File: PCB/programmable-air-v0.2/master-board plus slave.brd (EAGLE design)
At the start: 97.8 x 98.9 mm, 74 parts, among them IC2 INA126U, IC4 LM358MX, J1 POWER_JACKTOE, Q4 600mA/40V, Q5 600mA/40V, Q6 600mA/40V

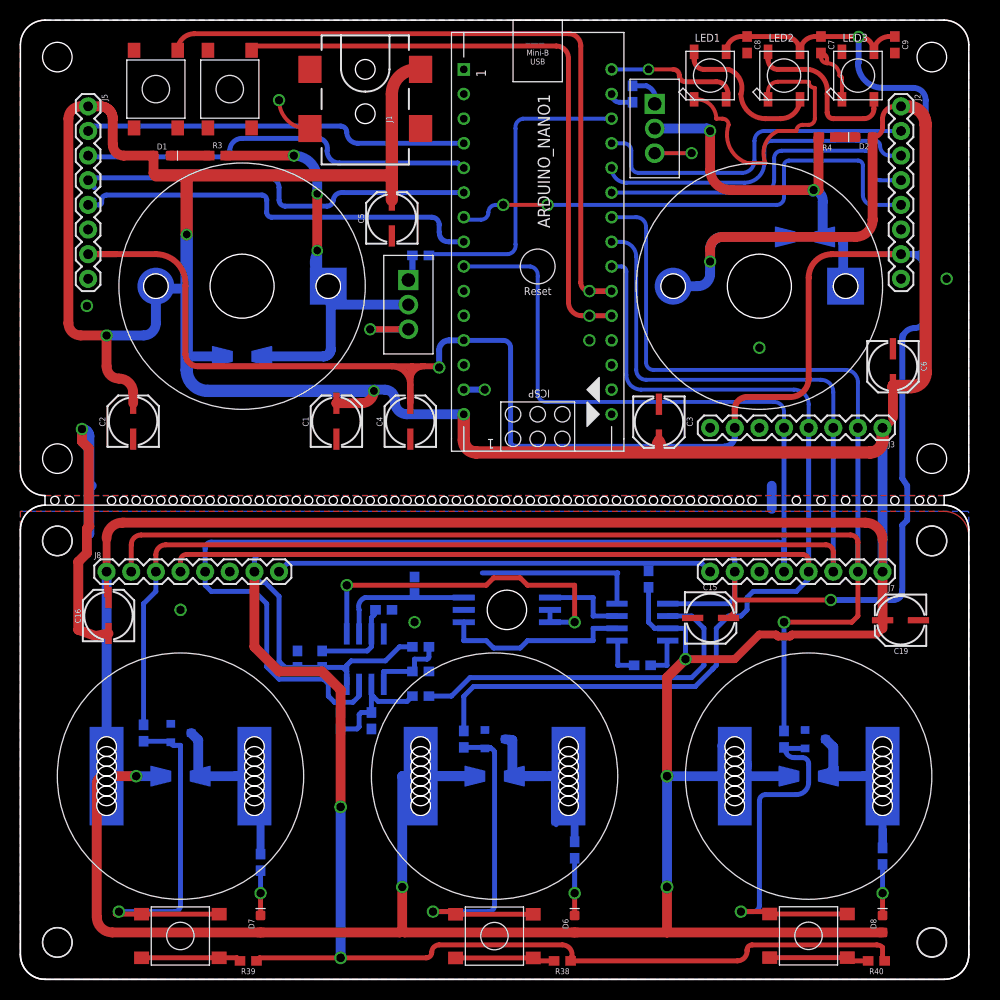
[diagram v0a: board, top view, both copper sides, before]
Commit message: Minor changes to the PCB
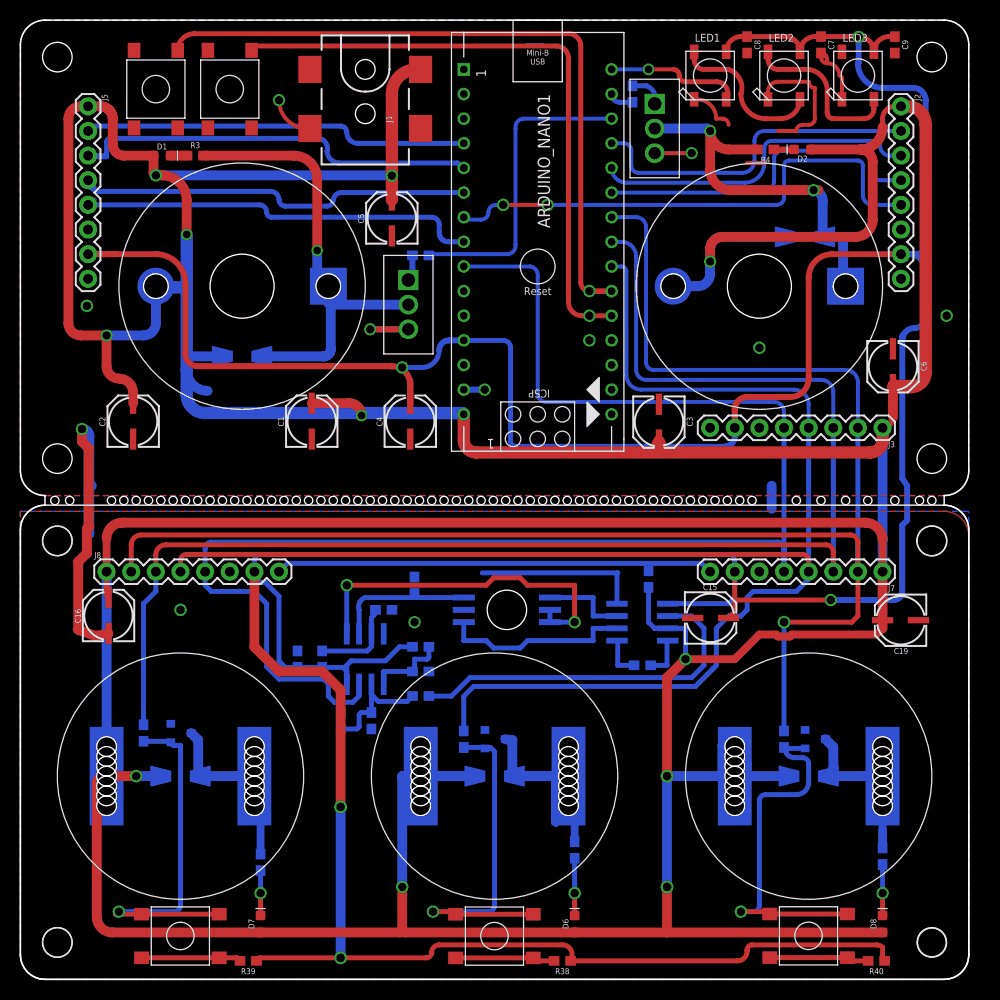
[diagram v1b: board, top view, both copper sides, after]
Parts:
- moved D2 6.48 mm to (80.6, 85.6)
- moved R4 6.48 mm to (76.8, 85.6)
- moved C1 2.54 mm to (29.8, 57.5)
- moved R3 2.29 mm to (18.0, 85.0)
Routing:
- net VCC: track 476.4 -> 468.2 mm
- net GND: track 171.0 -> 163.1 mm
- net VIN: track 797.3 -> 789.6 mm, vias 9 -> 11
- net N$11: track 41.0 -> 43.9 mm
- net N$12: track 3.99 -> 1.70 mm
- net N$14: track 47.5 -> 45.8 mm
- net N$18: track 42.3 -> 41.7 mm
- net N$5: track 49.3 -> 49.2 mm, vias 3 -> 1

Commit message: Sent PCBs for fabrication
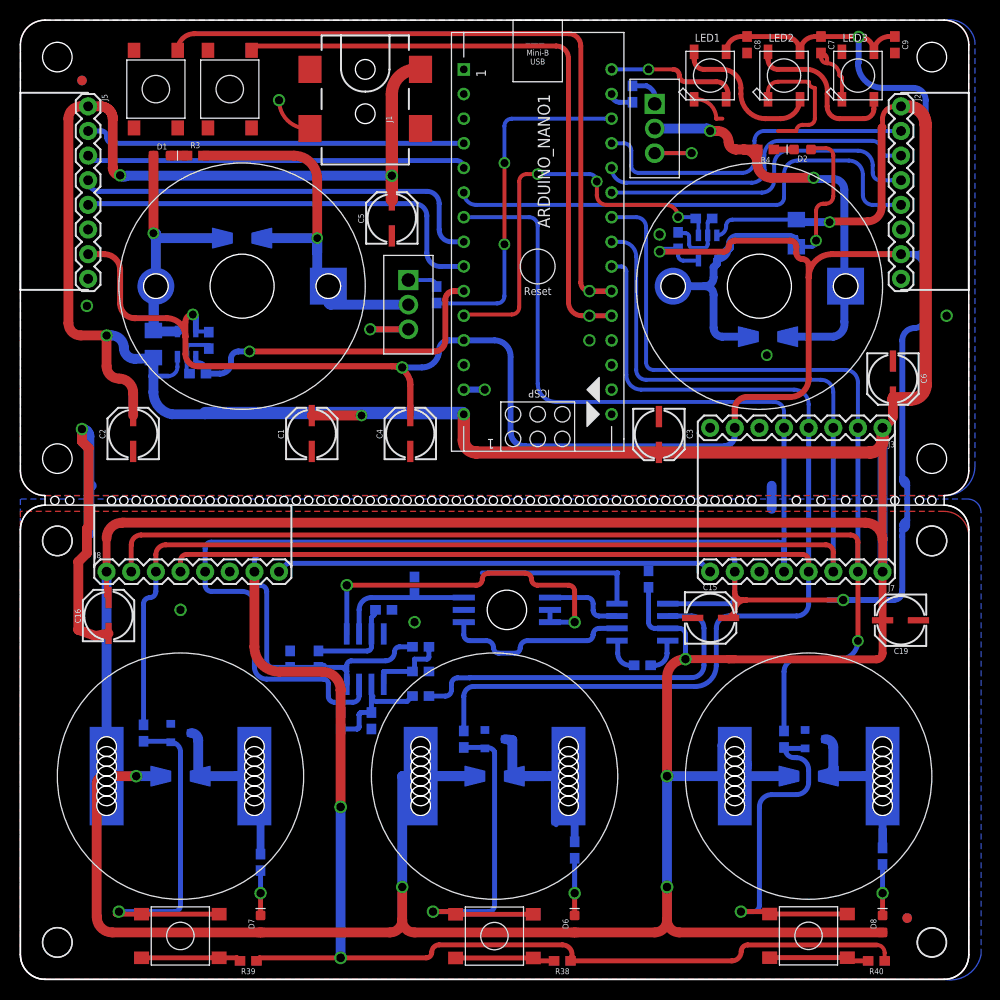
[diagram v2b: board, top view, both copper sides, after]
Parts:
- added C10, C11: 0.1uF, SparkFun-Passives:0603-CAP
- added R5, R7: (no value), SparkFun-Resistors:0603
- added R6, R8: (no value), SparkFun-Resistors:1206
- added U$10, U$11, U$12, U$9: FIDUCIAL, adafruit:FIDUCIAL_1MM
- added U1, U2: INA169, SparkFun-AnalogIC:SOT23-5
- R34: value 40K -> 10k
- R35, R36: value 20K -> 10k
- R37: value 2K -> 10k
- moved U$3 12.2 mm to (22.9, 76.5)
- moved U$4 11.0 mm to (77.1, 66.3)
- moved R1 4.39 mm to (42.9, 70.6), turned to 90 degrees
- moved C6 1.27 mm to (90.2, 62.0)
- moved C1 1.27 mm to (29.8, 56.3)
- moved C2 1.27 mm to (11.4, 56.3)
- moved C3 1.27 mm to (66.0, 56.3)
- moved C4 1.27 mm to (40.0, 56.3)
- moved C17 0.76 mm to (27.8, 33.0)
- moved R34 0.38 mm to (30.7, 33.0)
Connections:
- removed net N$64: J7.6, J8.6
- new net VIN-: D2.A, R6.2, U$2.P$1, U$4.P$1, U2.4
- new net VIN-1: D1.A, R8.2, U$1.P$1, U$3.P$1, U1.4
- new net VOUT: ARDUINO_NANO1.10, R7.2, U1.1
- new net VOUT1: ARDUINO_NANO1.11, R5.2, U2.1
- net GND: now also C10.1, C11.1, R5.1, R7.1, U1.2, U2.2
- net N$13: now also ARDUINO_NANO1.6; no longer ARDUINO_NANO1.7
- net N$14: now also ARDUINO_NANO1.9; no longer ARDUINO_NANO1.8
- net N$18: now also ARDUINO_NANO1.8; no longer ARDUINO_NANO1.6
- net N$63: now also ARDUINO_NANO1.7; no longer ARDUINO_NANO1.9
- net VCC: now also C10.2, C11.2, U1.5, U2.5
- net VIN: now also R6.1, R8.1, U1.3, U2.3; no longer D1.A, D2.A, U$1.P$1, U$2.P$1, U$3.P$1, U$4.P$1
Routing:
- net VIN: track 789.6 -> 719.0 mm, vias 11 -> 10
- net VIN-: track 0.00 -> 46.7 mm, vias 0 -> 1
- net VCC: track 468.2 -> 511.5 mm, vias 5 -> 7
- net VOUT1: track 0.00 -> 42.2 mm, vias 0 -> 3
- net VOUT: track 0.00 -> 35.3 mm, vias 0 -> 1
- net VIN-1: track 0.00 -> 33.2 mm, vias 0 -> 1
- net GND: track 163.1 -> 173.5 mm, vias 11 -> 12
- net N$5: track 49.2 -> 43.1 mm
- net N$6: track 39.8 -> 45.7 mm
- net N$11: track 43.9 -> 39.3 mm
- net N$63: track 157.3 -> 161.7 mm
- net N$10: track 32.5 -> 36.8 mm, vias 0 -> 2
- net N$14: track 45.8 -> 43.7 mm
- net N$62: track 165.2 -> 166.8 mm
- net N$18: track 41.7 -> 43.3 mm
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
